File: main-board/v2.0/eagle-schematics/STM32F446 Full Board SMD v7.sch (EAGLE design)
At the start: 275 parts, among them Q1 16MHz

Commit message: improved front pane v3
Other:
- note added: "VCO3340A"
- note added: "VCO3340B"
- note removed: "VCO3340A (with wave selection switch)"
- note removed: "VCO3340B (multiwave output)"
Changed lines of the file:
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@@
 <setting verticaltext="up"/>
 </settings>
-<grid distance="0.1" unitdist="inch" unit="inch" style="lines" multiple="1" display="no" altdistance="0.01" altunitdist="inch" altunit="inch"/>
+<grid distance="0.05" unitdist="inch" unit="inch" style="lines" multiple="1" display="no" altdistance="0.01" altunitdist="inch" altunit="inch"/>
 <layers>
 <layer number="1" name="Top" color="4" fill="1" visible="no" active="no"/>
@@
 <wire x1="-195.58" y1="373.38" x2="-563.88" y2="373.38" width="0.1524" layer="97"/>
 <wire x1="-563.88" y1="373.38" x2="-563.88" y2="513.08" width="0.1524" layer="97"/>
-<text x="-558.8" y="502.92" size="6.4516" layer="97">VCO3340B (multiwave output)</text>
+<text x="-558.8" y="502.92" size="6.4516" layer="97">VCO3340B</text>
 <wire x1="-563.88" y1="360.68" x2="-195.58" y2="360.68" width="0.1524" layer="97"/>
 <wire x1="-195.58" y1="360.68" x2="-195.58" y2="220.98" width="0.1524" layer="97"/>
 <wire x1="-195.58" y1="220.98" x2="-563.88" y2="220.98" width="0.1524" layer="97"/>
 <wire x1="-563.88" y1="220.98" x2="-563.88" y2="360.68" width="0.1524" layer="97"/>
-<text x="-558.8" y="350.52" size="6.4516" layer="97">VCO3340A (with wave selection switch)</text>
+<text x="-558.8" y="350.52" size="6.4516" layer="97">VCO3340A</text>
 <wire x1="119.38" y1="208.28" x2="223.52" y2="208.28" width="0.1524" layer="97"/>
 <wire x1="223.52" y1="208.28" x2="223.52" y2="144.78" width="0.1524" layer="97"/>
@@
 <pinref part="C19" gate="G$1" pin="1"/>
 <wire x1="-157.48" y1="298.45" x2="-111.76" y2="298.45" width="0.1524" layer="91"/>
-<wire x1="-170.18" y1="381" x2="-157.48" y2="379.73" width="0.1524" layer="91"/>
-<wire x1="-157.48" y1="379.73" x2="-157.48" y2="298.45" width="0.1524" layer="91"/>
+<wire x1="-170.18" y1="381" x2="-157.48" y2="381" width="0.1524" layer="91"/>
+<wire x1="-157.48" y1="381" x2="-157.48" y2="298.45" width="0.1524" layer="91"/>
 <pinref part="B1" gate="G$1" pin="P$1"/>
 </segment>

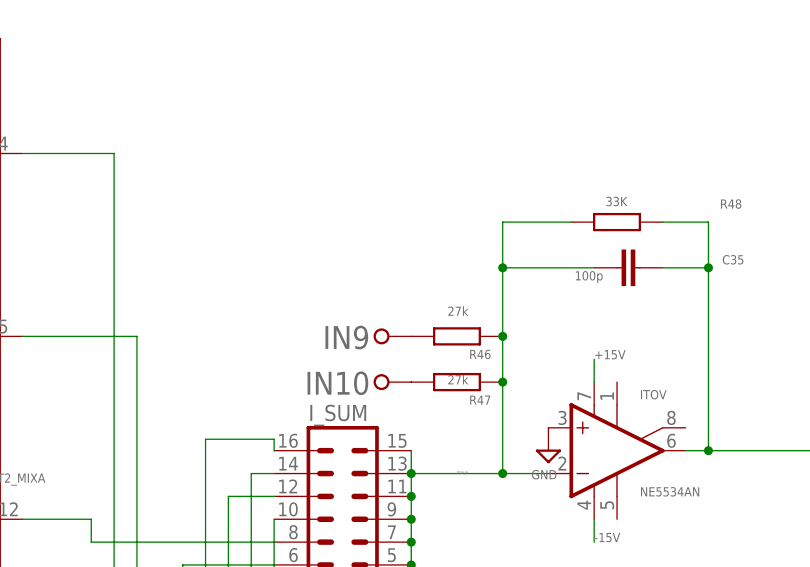
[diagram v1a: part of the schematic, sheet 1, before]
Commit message: Updated front pane
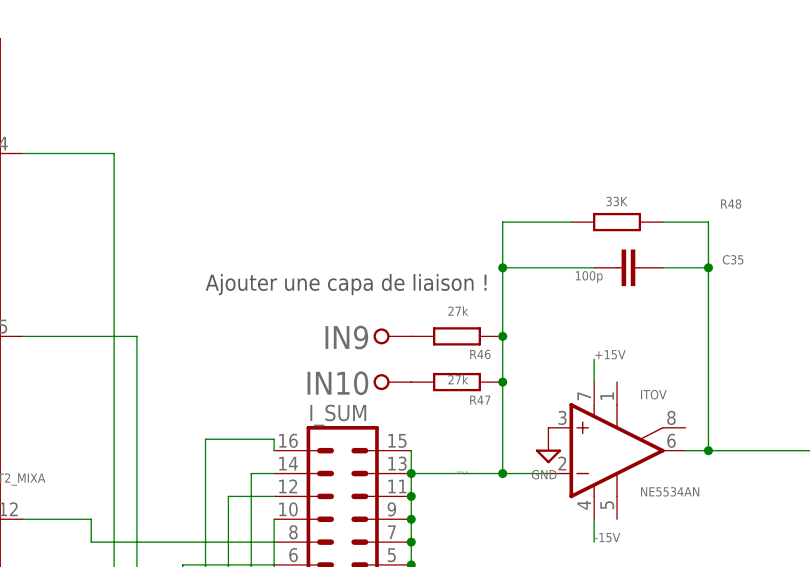
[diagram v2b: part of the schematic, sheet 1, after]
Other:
- note added: "Ajouter une capa de liaison !"
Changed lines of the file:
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@@
 <setting verticaltext="up"/>
 </settings>
-<grid distance="0.05" unitdist="inch" unit="inch" style="lines" multiple="1" display="no" altdistance="0.01" altunitdist="inch" altunit="inch"/>
+<grid distance="0.1" unitdist="inch" unit="inch" style="lines" multiple="1" display="no" altdistance="0.01" altunitdist="inch" altunit="inch"/>
 <layers>
 <layer number="1" name="Top" color="4" fill="1" visible="no" active="no"/>
@@
 - inverser le condo polarisé C54 (+ côté 0V et non côté -15V)
 - inverser la LED "-15V" (pour la même raison)</text>
+<text x="7.62" y="444.5" size="1.778" layer="97">Ajouter une capa de liaison !</text>
 </plain>
 <instances>

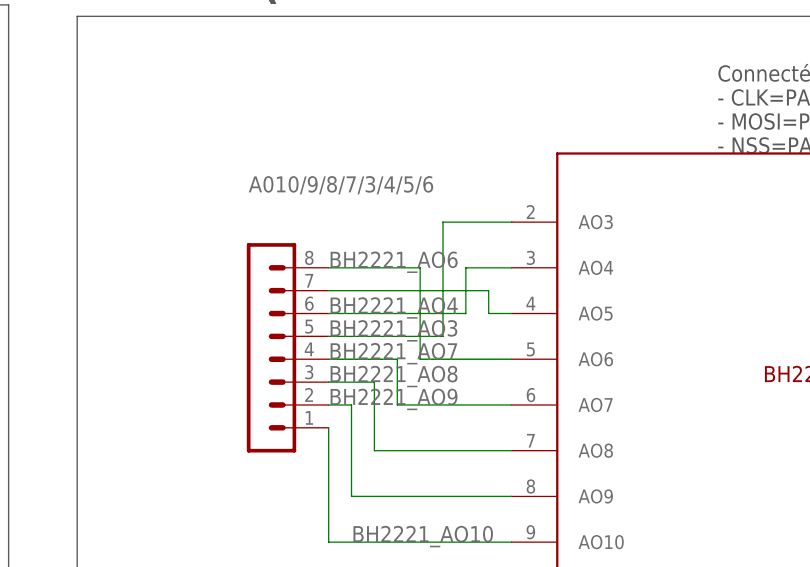
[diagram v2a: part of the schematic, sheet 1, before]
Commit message: Added missing net label on BH2221 DAC
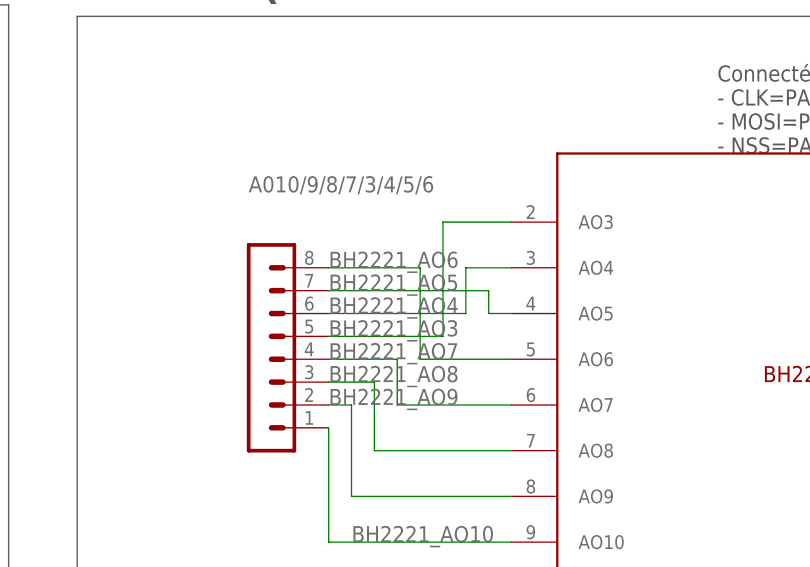
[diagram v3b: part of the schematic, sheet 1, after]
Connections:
- net N$23 renamed BH2221_AO5
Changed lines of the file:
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@@
 </segment>
 </net>
-<net name="N$23" class="0">
+<net name="BH2221_AO5" class="0">
 <segment>
 <pinref part="A010/9/8/7/3/4/5/6" gate="1" pin="7"/>
@@
 <wire x1="505.46" y1="246.38" x2="505.46" y2="243.84" width="0.1524" layer="91"/>
 <wire x1="505.46" y1="243.84" x2="508" y2="243.84" width="0.1524" layer="91"/>
+<label x="487.68" y="246.38" size="1.778" layer="95"/>
 </segment>
 </net>

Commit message: pointing new errors on the board layout
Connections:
- net N$34 renamed AD5644_A
- net N$35 renamed AD5644_B
- net N$39 renamed AD5644_C
- net N$40 renamed AD5644_D
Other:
- note added: "BUG: IN_VCFORDER's CONNECTED TO NOTHING!"
- note added: "MASSE ????"
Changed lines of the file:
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@@
 <wire x1="119.38" y1="144.78" x2="119.38" y2="208.28" width="0.1524" layer="97"/>
 <text x="119.38" y="137.16" size="6.4516" layer="97">MOD RING</text>
-<text x="152.4" y="322.58" size="5.08" layer="97">!!!! Erreurs de routage à corriger !!!!
+<text x="152.4" y="322.58" size="5.08" layer="105">!!!! Erreurs de routage à corriger !!!!
 Au moment de l'équipement de la carte :
 - inverser le condo polarisé C54 (+ côté 0V et non côté -15V)
 - inverser la LED "-15V" (pour la même raison)</text>
-<text x="7.62" y="444.5" size="1.778" layer="97">Ajouter une capa de liaison !</text>
+<text x="7.62" y="444.5" size="5.08" layer="105">Ajouter une capa de liaison !</text>
+<text x="259.08" y="515.62" size="1.778" layer="105">BUG: IN_VCFORDER's CONNECTED TO NOTHING!</text>
+<text x="-309.88" y="467.36" size="1.778" layer="105">MASSE ????</text>
 </plain>
 <instances>
@@
 </segment>
 </net>
-<net name="N$34" class="0">
+<net name="AD5644_A" class="0">
 <segment>
 <pinref part="AD5644" gate="G$0" pin="VOUTA"/>
@@
 </segment>
 </net>
-<net name="N$35" class="0">
+<net name="AD5644_B" class="0">
 <segment>
 <pinref part="ABCD" gate="1" pin="2"/>
@@
 </segment>
 </net>
-<net name="N$39" class="0">
+<net name="AD5644_C" class="0">
 <segment>
 <pinref part="AD5644" gate="G$0" pin="VOUTC"/>
@@
 </segment>
 </net>
-<net name="N$40" class="0">
+<net name="AD5644_D" class="0">
 <segment>
 <pinref part="ABCD" gate="1" pin="4"/>

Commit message: changed DAC pin assignement
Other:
- note added: "Channels: A01-12 = 8 bits B01-04 = 14 bits - A03-04 & A07-12 : 2164D vca - A06 : VCF cutoff - A05 : VCF Q - A02 : PWM 3340A - A01 : PWM 3340B - B01 : CV 3340A - B02 : CV 3340B - B03 : noise / wave generator (VCO #3) - B04 : VCA LM13700"
- note removed: "Channels: A01-12 = 8 bits B01-04 = 14 bits - A01 à A08 : 2164D vca - A09 : VCF cutoff - A10 : VCF Q - A11 : PWM 3340A - A12 : PWM 3340B - B01 : CV 3340A - B02 : CV 3340B - B03 : noise / wave generator (VCO #3) - B04 : VCA LM13700"
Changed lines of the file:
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@@
 A01-12 = 8 bits
 B01-04 = 14 bits
-- A01 à A08 : 2164D vca
-- A09 : VCF cutoff
-- A10 : VCF Q
-- A11 : PWM 3340A
-- A12 : PWM 3340B
+- A03-04 &amp; A07-12 : 2164D vca
+- A06 : VCF cutoff
+- A05 : VCF Q
+- A02 : PWM 3340A
+- A01 : PWM 3340B
 - B01 : CV 3340A
 - B02 : CV 3340B
@@
 <segment>
 <wire x1="271.78" y1="508" x2="271.78" y2="500.38" width="0.1524" layer="91"/>
-<label x="274.32" y="508" size="1.016" layer="95"/>
+<label x="274.32" y="500.38" size="1.016" layer="95"/>
 <pinref part="R68" gate="G$1" pin="2"/>
 <pinref part="ADG453" gate="G$1" pin="IN1"/>
